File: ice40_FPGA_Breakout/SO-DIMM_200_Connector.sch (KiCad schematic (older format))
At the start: 0 parts

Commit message: FTDI, iCE40 chip differential pair schematic
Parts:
- added R? (x60): R, symbol R
- added TP? (x8): Test_Point, symbol Test_Point
- added U? (x4): iCE40HX8_CT256, symbol iCE40HX8_CT256
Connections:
- new net: R?.1, U?.B1 (IOL_2B)
- new net: R?.1, U?.B2 (IOL_1B)
- new net: R?.1, U?.C1 (IOL_3A)
- new net: R?.1, U?.C2 (IOL_3B)
- new net: R?.1, U?.D1 (IOL_5B)
- new net: R?.1, U?.D2 (IOL_4B)
- new net: R?.1, U?.E2 (IOL_7B)
- new net: R?.1, U?.E3 (IOL_6B)
- new net: R?.1, U?.E4 (IOL_1A)
- new net: R?.1, U?.F1 (IOL_10B)
- new net: R?.1, U?.F2 (IOL_9B)
- new net: R?.1, U?.F3 (IOL_8B)
- new net: R?.1, U?.F4 (IOL_4A)
- new net: R?.1, U?.F5 (IOL_2A)
- new net: TP?.1, U?.G1 (IOL_13B_GBIN7)
- new net: R?.1, U?.G2 (IOL_11B)
- new net: R?.1, U?.G3 (IOL_8A)
- new net: R?.1, U?.G4 (IOL_6A)
- new net: R?.1, U?.G5 (IOL_5A)
- new net: TP?.1, U?.H1 (IOL_14B)
- new net: R?.1, U?.H2 (IOL_12B)
- new net: R?.1, U?.H3 (IOL_9A)
- new net: R?.1, U?.H4 (IOL_11A)
- new net: R?.1, U?.H5 (IOL_7A)
- new net: R?.1, U?.H6 (IOL_10A)
- new net: R?.1, U?.J1 (IOL_15B)
- new net: R?.1, U?.J2 (IOL_15A)
- new net: TP?.1, U?.J3 (IOL_14A_GBIN6)
- new net: R?.1, U?.J4 (IOL_12A)
- new net: TP?.1, U?.J5 (IOL_13A)
- new net: R?.2, U?.K1 (IOL_16A)
- new net: R?.2, U?.K3 (IOL_16B)
- new net: R?.2, U?.K4 (IOL_18A)
- new net: R?.2, U?.K5 (IOL_20A)
- new net: R?.2, U?.L1 (IOL_17B)
- new net: R?.2, U?.L3 (IOL_19B)
- new net: R?.2, U?.L4 (IOL_17A)
- new net: R?.2, U?.L6 (IOL_19A)
- new net: R?.2, U?.L7 (IOL_21A)
- new net: R?.2, U?.M1 (IOL_18B)
- new net: R?.2, U?.M2 (IOL_20B)
- new net: R?.2, U?.M3 (IOL_22B)
- new net: R?.2, U?.M6 (IOL_22A)
- new net: R?.2, U?.N2 (IOL_21B)
- new net DPIO_1+: R?.2, R?.2
- new net DPIO_1-: R?.1, R?.2
- new net DPIO_10+: R?.2
- new net DPIO_10-: R?.1, R?.2
- new net DPIO_11+: R?.2, R?.2
- new net DPIO_11-: R?.1, R?.2
- new net DPIO_12+: R?.2, R?.2
- new net DPIO_12-: R?.1, R?.2
- new net DPIO_13+: R?.1, R?.2
- new net DPIO_13-: R?.2
- new net DPIO_14+: R?.1
- new net DPIO_14-: R?.1, R?.2
- new net DPIO_15+: R?.1, R?.1
- new net DPIO_15-: R?.1, R?.2
- new net DPIO_16+: R?.1, R?.1
- new net DPIO_16-: R?.1, R?.2
- new net DPIO_17+: R?.1, R?.1
- new net DPIO_17-: R?.1, R?.2
- new net DPIO_18+: R?.1, R?.1
- new net DPIO_18-: R?.1, R?.2
- new net DPIO_19+: R?.1, R?.1, TP?.1
- new net DPIO_19-: R?.1, R?.2, TP?.1
- new net DPIO_2+: R?.2, R?.2
- new net DPIO_2-: R?.1, R?.2
- new net DPIO_20+: R?.1, R?.1, TP?.1
- new net DPIO_20-: R?.1, R?.2, TP?.1
- new net DPIO_3+: R?.2
- new net DPIO_3-: R?.1, R?.2
- new net DPIO_4+: R?.2, R?.2
- new net DPIO_4-: R?.1, R?.2
- new net DPIO_5+: R?.2, R?.2
- new net DPIO_5-: R?.1, R?.2
- new net DPIO_6+: R?.2, R?.2
- new net DPIO_6-: R?.1, R?.2
- new net DPIO_7+: R?.2, R?.2
- new net DPIO_7-: R?.1, R?.2
- new net DPIO_8+: R?.2, R?.2
- new net DPIO_8-: R?.1, R?.2
- new net DPIO_9+: R?.2, R?.2
- new net DPIO_9-: R?.1, R?.2

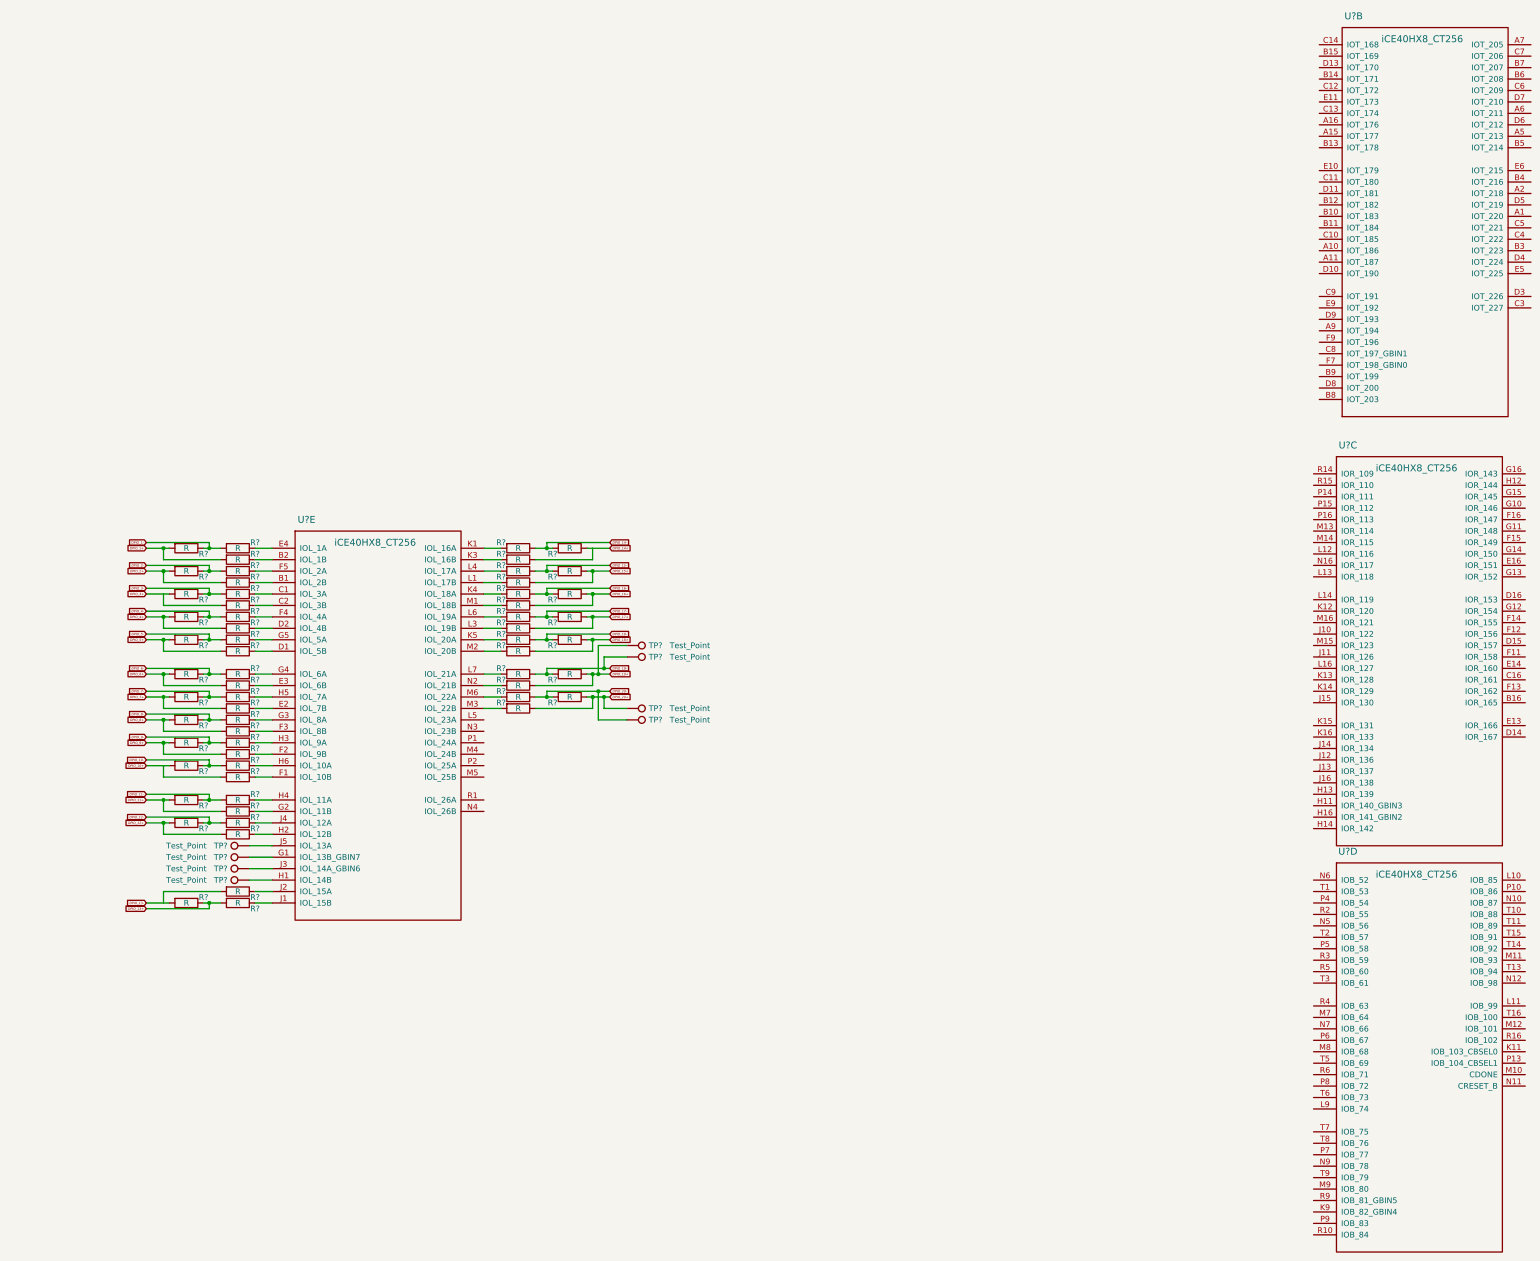
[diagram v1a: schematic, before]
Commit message: Added SO-DIMM header, ice40 IO and FTDI power
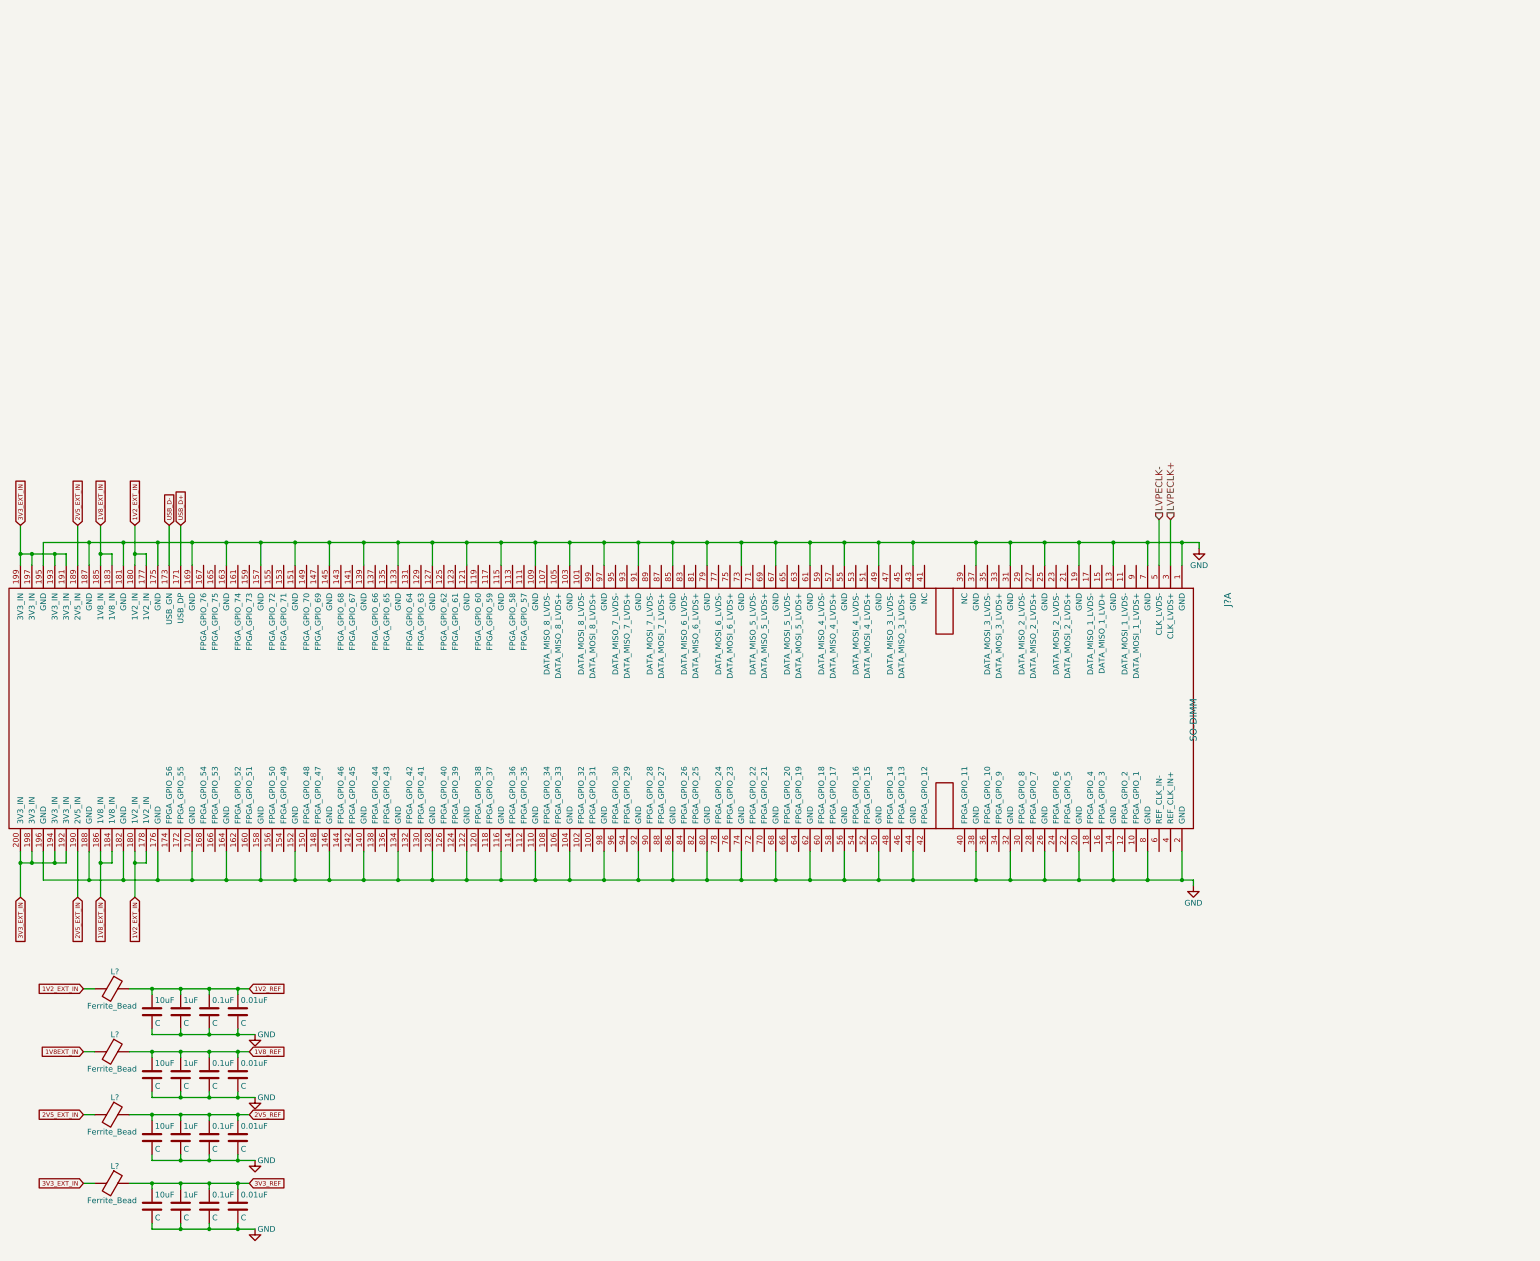
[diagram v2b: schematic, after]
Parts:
- removed R? (x60): R, symbol R
- removed TP? (x8): Test_Point, symbol Test_Point
- removed U? (x4): iCE40HX8_CT256, symbol iCE40HX8_CT256
- added 0.01uF (x4), 0.1uF (x4), 10uF (x4), 1uF (x4): C, symbol C
- added J?: SO-DIMM, symbol SO-DIMM
- added L? (x4): Ferrite_Bead, symbol Ferrite_Bead
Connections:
- new net 1V2_EXT_IN: J?.177 (1V2_IN), J?.178 (1V2_IN), J?.180 (1V2_IN), L?.2
- new net 1V2_REF: 0.01uF.1, 0.1uF.1, 10uF.1, 1uF.1, L?.1
- new net 1V8EXT_IN: L?.2
- new net 1V8_EXT_IN: J?.183 (1V8_IN), J?.184 (1V8_IN), J?.185 (1V8_IN), J?.186 (1V8_IN)
- new net 1V8_REF: 0.01uF.1, 0.1uF.1, 10uF.1, 1uF.1, L?.1
- new net 2V5_EXT_IN: J?.189 (2V5_IN), J?.190 (2V5_IN), L?.2
- new net 2V5_REF: 0.01uF.1, 0.1uF.1, 10uF.1, 1uF.1, L?.1
- new net 3V3_EXT_IN: J?.191 (3V3_IN), J?.192 (3V3_IN), J?.193 (3V3_IN), J?.194 (3V3_IN), J?.197 (3V3_IN), J?.198 (3V3_IN), J?.199 (3V3_IN), J?.200 (3V3_IN), L?.2
- new net 3V3_REF: 0.01uF.1, 0.1uF.1, 10uF.1, 1uF.1, L?.1
- new net GND: 0.01uF.2, 0.01uF.2, 0.01uF.2, 0.01uF.2, 0.1uF.2, 0.1uF.2, 0.1uF.2, 0.1uF.2, 10uF.2, 10uF.2, 10uF.2, 10uF.2, 1uF.2, 1uF.2, 1uF.2, 1uF.2, J?.1 (GND), J?.103 (GND), J?.104 (GND), J?.109 (GND), J?.110 (GND), J?.115 (GND), J?.116 (GND), J?.121 (GND), J?.122 (GND), J?.127 (GND), J?.128 (GND), J?.13 (GND), J?.133 (GND), J?.134 (GND), J?.139 (GND), J?.14 (GND), J?.140 (GND), J?.145 (GND), J?.146 (GND), J?.151 (GND), J?.152 (GND), J?.157 (GND), J?.158 (GND), J?.163 (GND), J?.164 (GND), J?.169 (GND), J?.170 (GND), J?.175 (GND), J?.176 (GND), J?.181 (GND), J?.182 (GND), J?.187 (GND), J?.188 (GND), J?.19 (GND), J?.195 (GND), J?.196 (GND), J?.2 (GND), J?.20 (GND), J?.25 (GND), J?.26 (GND), J?.31 (GND), J?.32 (GND), J?.37 (GND), J?.38 (GND), J?.43 (GND), J?.44 (GND), J?.49 (GND), J?.50 (GND), J?.55 (GND), J?.56 (GND), J?.61 (GND), J?.62 (GND), J?.67 (GND), J?.68 (GND), J?.7 (GND), J?.73 (GND), J?.74 (GND), J?.79 (GND), J?.8 (GND), J?.80 (GND), J?.85 (GND), J?.86 (GND), J?.91 (GND), J?.92 (GND), J?.97 (GND), J?.98 (GND)
- new net LVPECLK+: J?.3 (CLK_LVDS+)
- new net LVPECLK-: J?.5 (CLK_LVDS-)
- new net USB_D+: J?.171 (USB_DP)
- new net USB_D-: J?.173 (USB_GN)

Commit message: Add SPI EEPROM logic for SPI switching
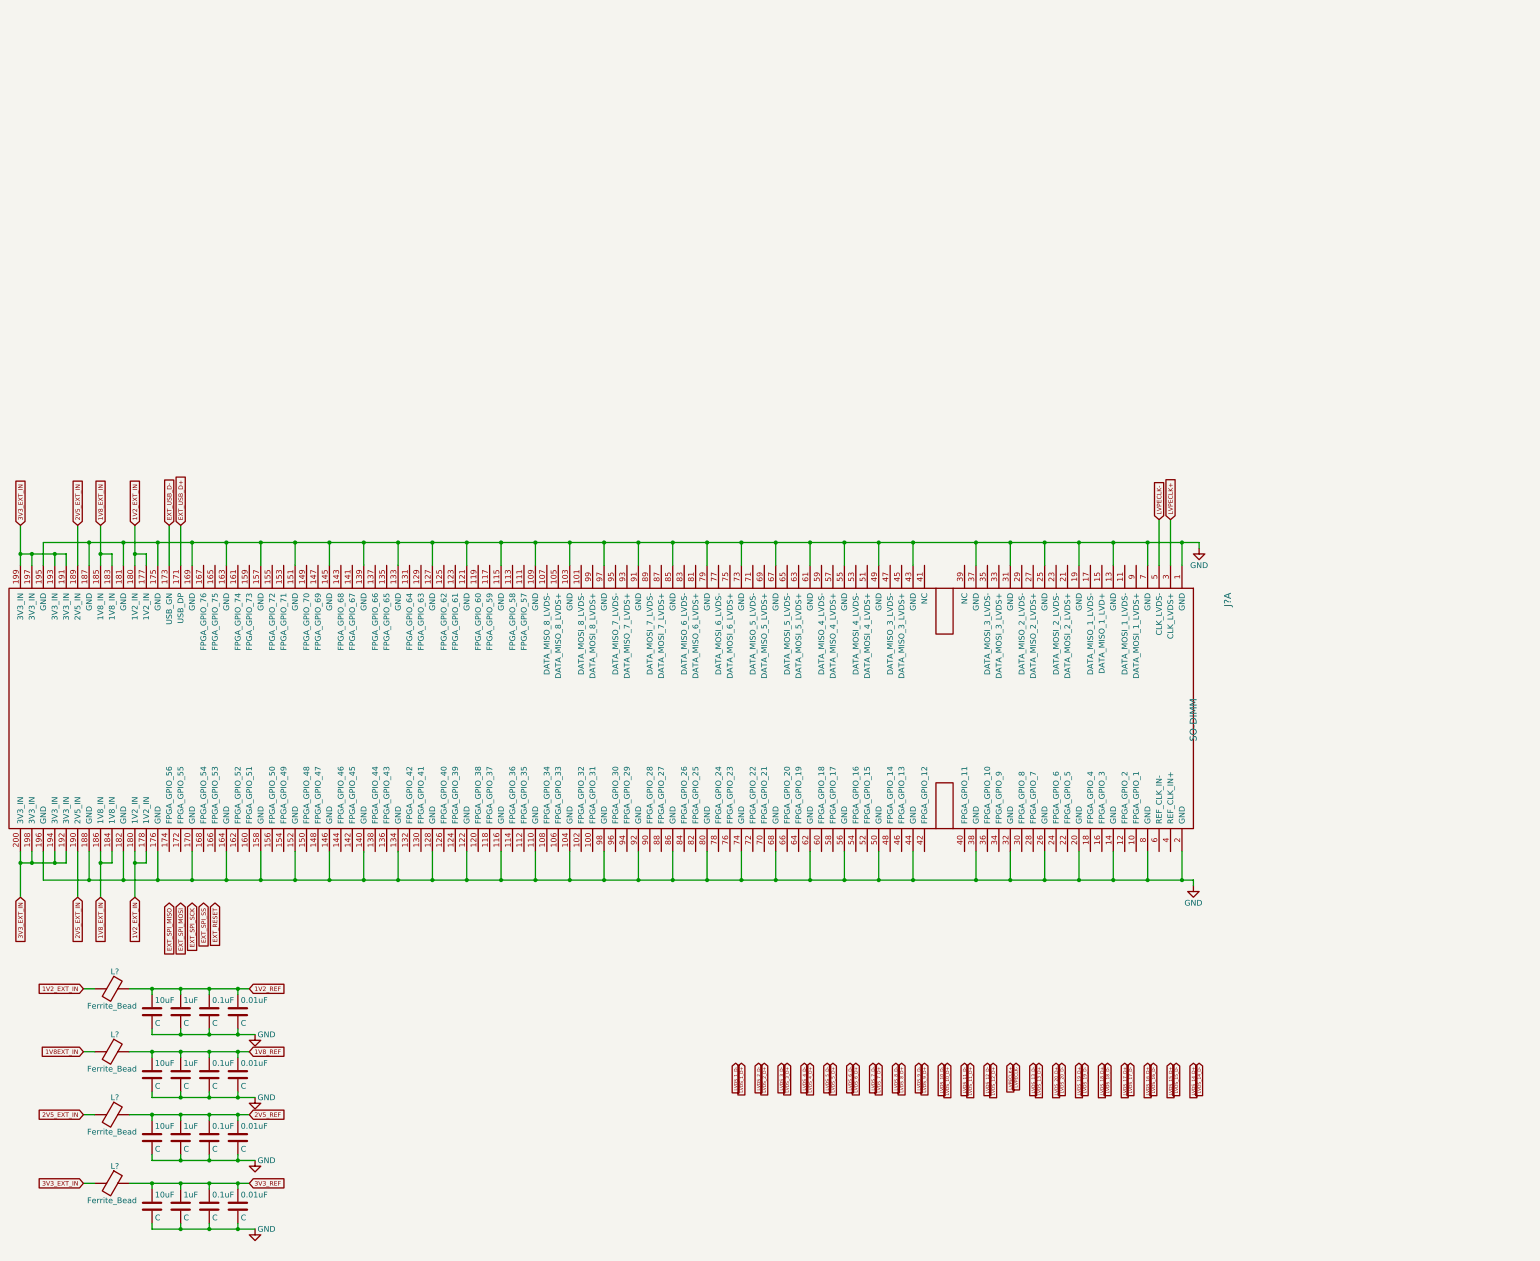
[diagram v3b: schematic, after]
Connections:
- net USB_D+ renamed EXT_USB_D+
- net USB_D- renamed EXT_USB_D-
